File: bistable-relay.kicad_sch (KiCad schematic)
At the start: 11 parts, among them J1 edge_connector, K1 Fujitsu_FTR-F1A, U1 MIC4427

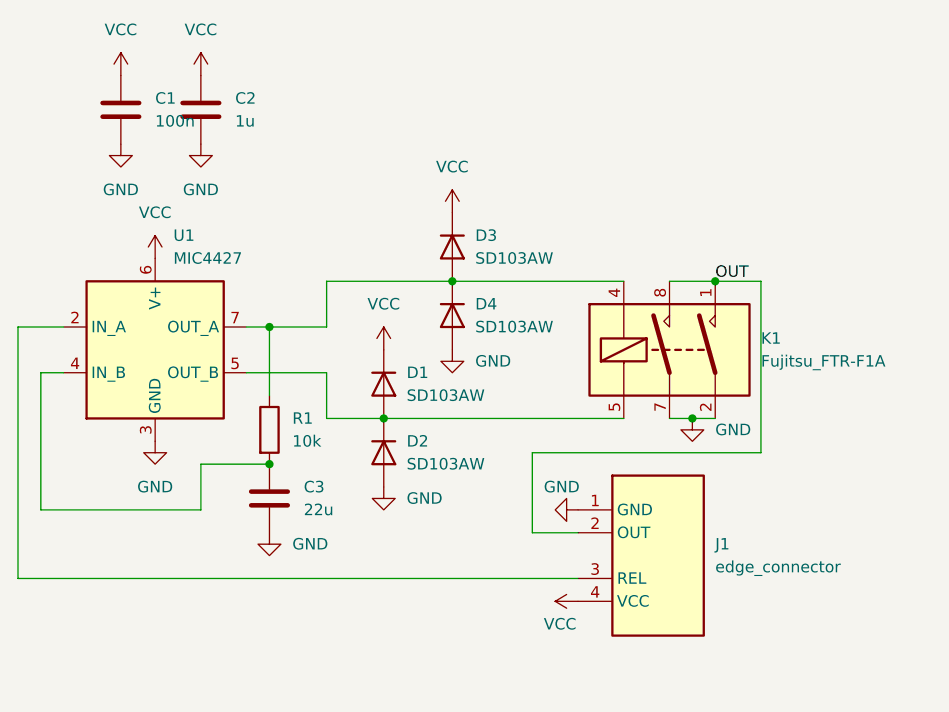
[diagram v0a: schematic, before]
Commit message: use FH44L relay
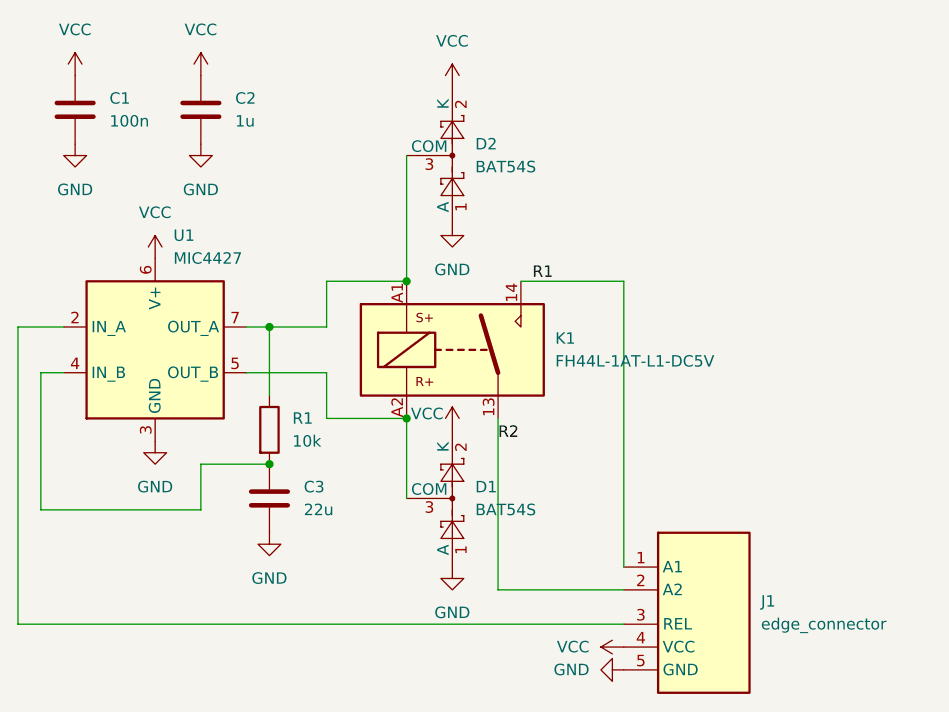
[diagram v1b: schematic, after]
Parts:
- removed D1, D2, D3, D4: SD103AW, Diode_SMD:D_SOD-123F, symbol Diode:1N4148W
- removed K1: Fujitsu_FTR-F1A, Relay_THT:Relay_DPST_Fujitsu_FTR-F1A, symbol Relay:Fujitsu_FTR-F1A
- added D1, D2: BAT54S, Package_TO_SOT_SMD:SOT-23, symbol Diode:BAT54S
- added K1: FH44L-1AT-L1-DC5V, Library:RELAY-TH_FH44L-1AT-L1-DC5V, symbol library:Relay_SPST_Latching_1coil
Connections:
- net GND: now also J1.5 (GND), D1.1 (A), D2.1 (A); no longer J1.1 (GND)
- net VCC: now also D1.2 (K), D2.2 (K)
- net at R1.1, U1.7 (OUT_A): now also D2.3 (COM), K1.A1
- net at U1.5 (OUT_B): now also D1.3 (COM), K1.A2
- net OUT renamed R2
- net R2: now also K1.13
- new net R1: J1.1 (A1), K1.14
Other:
- moved on the sheet: C1

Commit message: change 100nF capacitor to 0402 package
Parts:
- C1: footprint Capacitor_SMD:C_0603_1608Metric -> Capacitor_SMD:C_0402_1005Metric
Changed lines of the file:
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@@
 			)
 		)
-		(property "Footprint" "Capacitor_SMD:C_0603_1608Metric"
+		(property "Footprint" "Capacitor_SMD:C_0402_1005Metric"
 			(at 108.9152 73.66 0)
 			(effects
